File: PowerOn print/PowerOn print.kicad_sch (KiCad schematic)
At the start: 10 parts, among them P1 USB_C_Plug_USB2.0, P2 USB_C_Plug_USB2.0, Q1 FQP27P06, Q2 2N3904, SW1 SW_DIP_x01

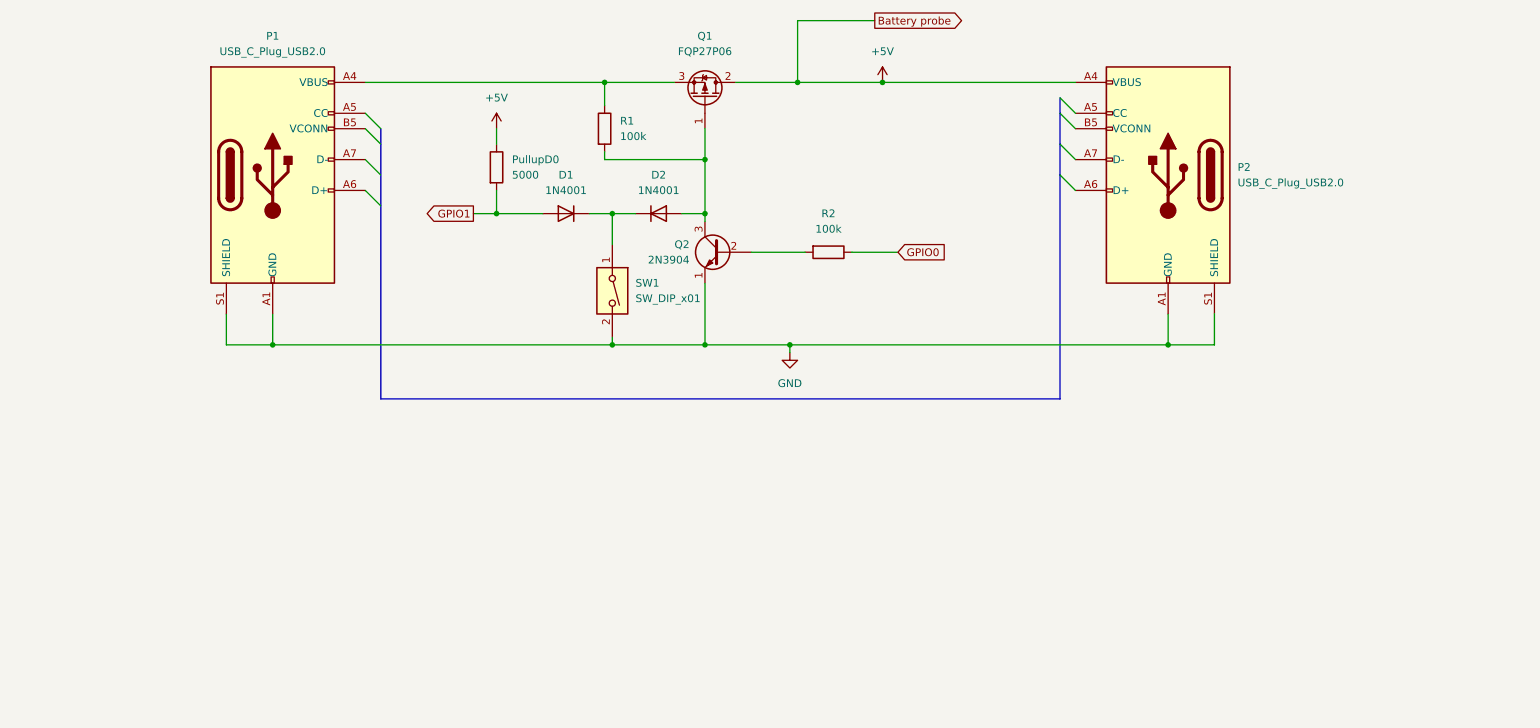
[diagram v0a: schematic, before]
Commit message: Redesign Poweron system
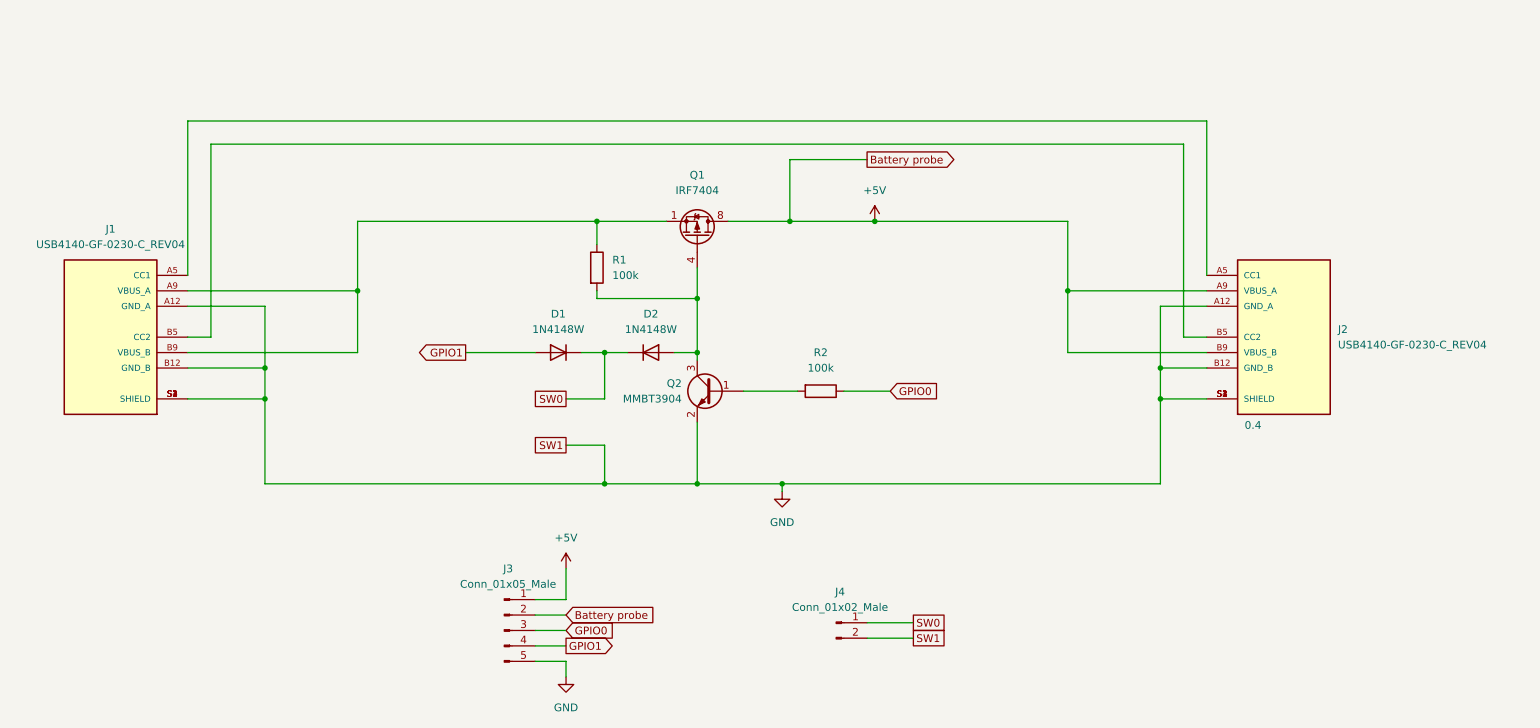
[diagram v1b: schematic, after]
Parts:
- removed D1, D2: 1N4001, Diode_THT:D_DO-41_SOD81_P10.16mm_Horizontal, symbol Diode:1N4001
- removed P1, P2: USB_C_Plug_USB2.0, symbol Connector:USB_C_Plug_USB2.0
- removed PullupD0: 5000, symbol Device:R
- removed Q1: FQP27P06, Package_TO_SOT_THT:TO-220-3_Vertical, symbol Transistor_FET:FQP27P06
- removed Q2: 2N3904, Package_TO_SOT_THT:TO-92_Inline, symbol Transistor_BJT:2N3904
- removed SW1: SW_DIP_x01, symbol Switch:SW_DIP_x01
- added D1, D2: 1N4148W, Diode_SMD:D_SOD-123, symbol Diode:1N4148W
- added J1, J2: USB4140-GF-0230-C_REV04, GCT_USB4140-GF-0230-C_REV0.4, symbol USB4140-GF-0230-C_REV0.4:USB4140-GF-0230-C_REV0.4
- added J3: Conn_01x05_Male, Connector_PinHeader_1.00mm:PinHeader_1x05_P1.00mm_Vertical, symbol Connector:Conn_01x05_Male
- added J4: Conn_01x02_Male, Connector_PinHeader_1.00mm:PinHeader_1x02_P1.00mm_Vertical, symbol Connector:Conn_01x02_Male
- added Q1: IRF7404, Package_SO:SOIC-8_3.9x4.9mm_P1.27mm, symbol Transistor_FET:IRF7404
- added Q2: MMBT3904, Package_TO_SOT_SMD:SOT-23, symbol Transistor_BJT:MMBT3904
- R1, R2: footprint (none) -> Resistor_SMD:R_0805_2012Metric
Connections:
- net +5V: now also J2.A9 (VBUS_A), J2.B9 (VBUS_B), J3.1 (Pin_1), J3.2 (Pin_2), Q1.5 (D), Q1.6 (D), Q1.7 (D), Q1.8 (D)
- net GND: now also J1.A12 (GND_A), J1.B12 (GND_B), J1.S1 (SHIELD), J1.S2 (SHIELD), J1.S3 (SHIELD), J1.S4 (SHIELD), J2.A12 (GND_A), J2.B12 (GND_B), J2.S1 (SHIELD), J2.S2 (SHIELD), J2.S3 (SHIELD), J2.S4 (SHIELD), J3.5 (Pin_5), J4.2 (Pin_2), Q2.2 (E)
- net GPIO0: now also J3.3 (Pin_3)
- net GPIO1: now also D1.2 (A), J3.4 (Pin_4)
- net at R1.2: now also D2.2 (A), Q1.4 (G), Q2.3 (C)
- net at R1.1: now also J1.A9 (VBUS_A), J1.B9 (VBUS_B), Q1.1 (S), Q1.2 (S), Q1.3 (S)
- net at R2.2: now also Q2.1 (B)
- new net: J1.A5 (CC1), J2.A5 (CC1)
- new net: J1.B5 (CC2), J2.B5 (CC2)
- new net SW0: D1.1 (K), D2.1 (K), J4.1 (Pin_1)
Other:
- moved on the sheet: R1, R2

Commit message: PCB-Poweron-print-only
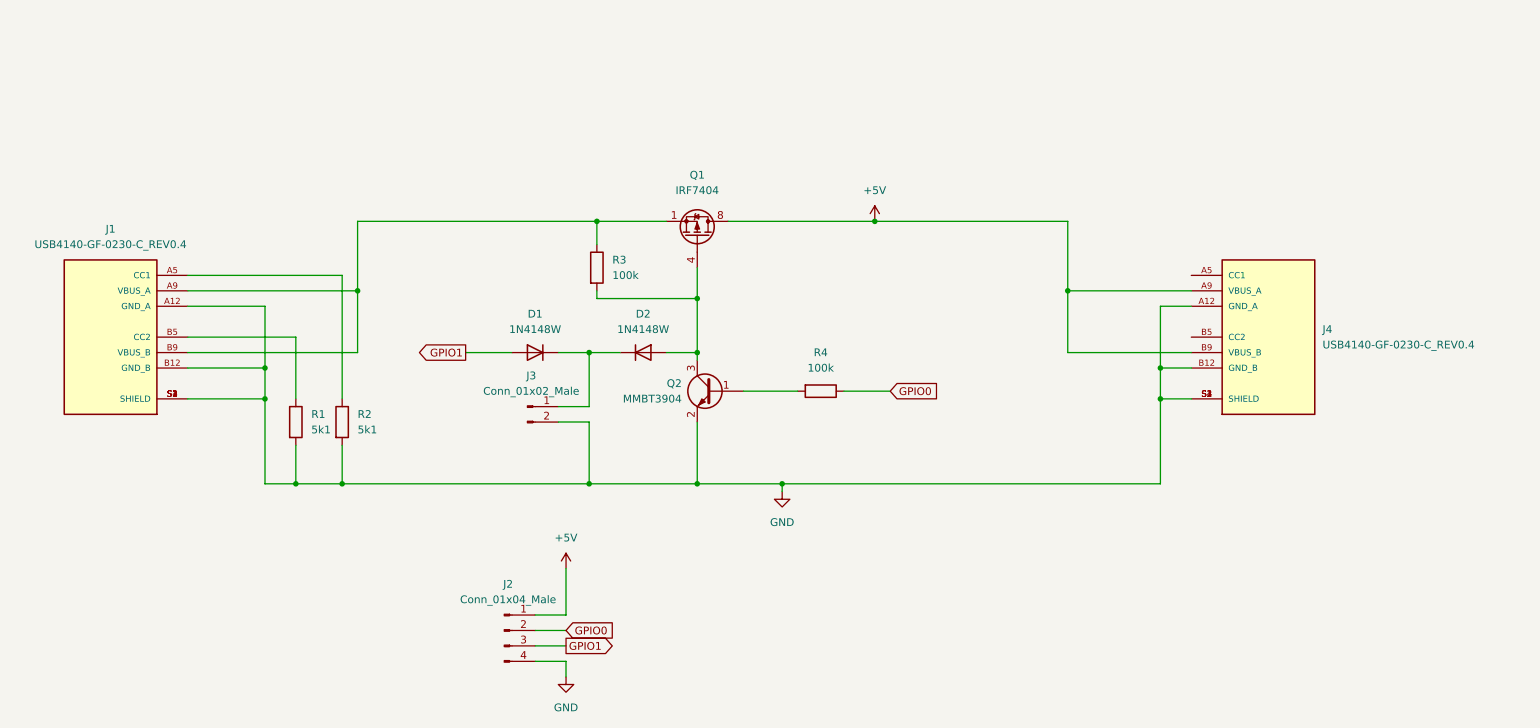
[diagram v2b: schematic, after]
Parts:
- removed J2: USB4140-GF-0230-C_REV04, GCT_USB4140-GF-0230-C_REV0.4, symbol USB4140-GF-0230-C_REV0.4:USB4140-GF-0230-C_REV0.4
- removed J3: Conn_01x05_Male, Connector_PinHeader_1.00mm:PinHeader_1x05_P1.00mm_Vertical, symbol Connector:Conn_01x05_Male
- added J2: Conn_01x04_Male, Connector_PinHeader_2.54mm:PinHeader_1x04_P2.54mm_Vertical, symbol Connector:Conn_01x04_Male
- added J4: USB4140-GF-0230-C_REV0.4, GCT_USB4140-GF-0230-C_REV0.4, symbol USB4140-GF-0230-C_REV0.4:USB4140-GF-0230-C_REV0.4
- added R1, R2: 5k1, Resistor_SMD:R_0805_2012Metric, symbol Device:R
- J1: value USB4140-GF-0230-C_REV04 -> USB4140-GF-0230-C_REV0.4
- J3: renamed from J4; footprint Connector_PinHeader_1.00mm:PinHeader_1x02_P1.00mm_Vertical -> Connector_PinHeader_2.54mm:PinHeader_1x02_P2.54mm_Vertical
- renumbered R1 to R3, R2 to R4
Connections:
- net +5V: now also J2.1 (Pin_1), J4.A9 (VBUS_A), J4.B9 (VBUS_B)
- net GND: now also J2.4 (Pin_4), J4.A12 (GND_A), J4.B12 (GND_B), J4.S1 (SHIELD), J4.S2 (SHIELD), J4.S3 (SHIELD), J4.S4 (SHIELD), R1.2, R2.2
- net GPIO0: now also J2.2 (Pin_2)
- net GPIO1: now also J2.3 (Pin_3)
- net at J1.A5 (CC1): now also R2.1
- net at J1.B5 (CC2): now also R1.1
- net SW0: no longer names the net of D1.1 (K), D2.1 (K), J3.1 (Pin_1)
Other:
- moved on the sheet: D1, D2, J3

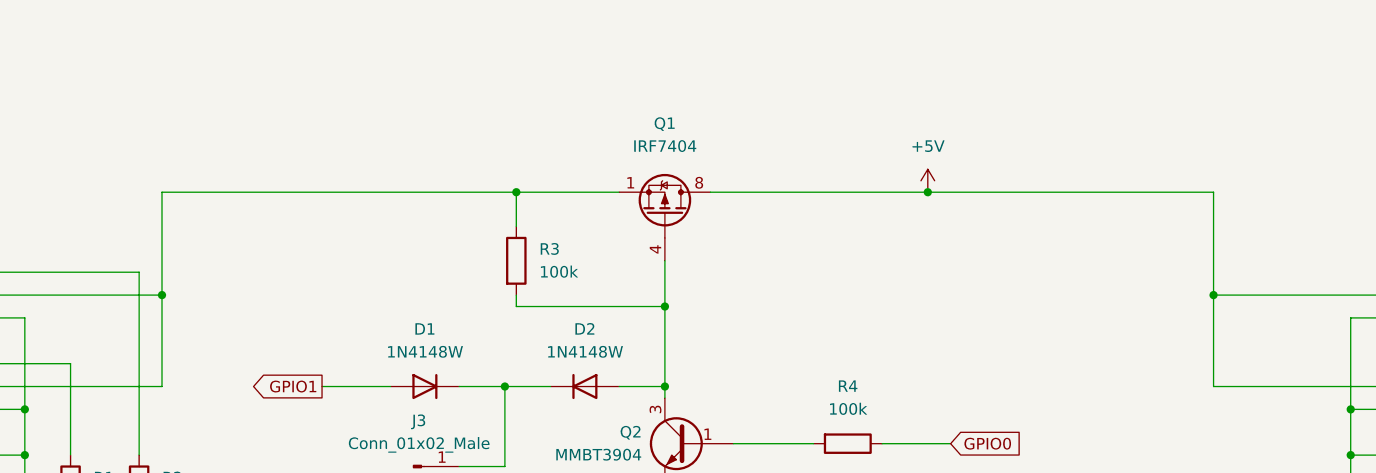
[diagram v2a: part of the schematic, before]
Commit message: Poweron print adapted
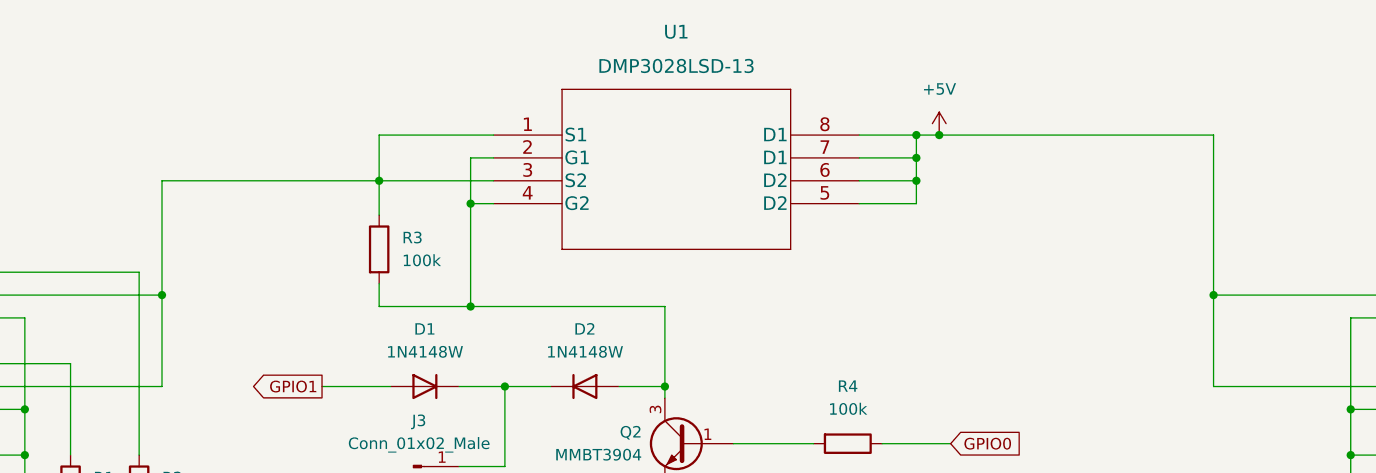
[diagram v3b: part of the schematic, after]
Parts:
- removed Q1: IRF7404, Package_SO:SOIC-8_3.9x4.9mm_P1.27mm, symbol Transistor_FET:IRF7404
- added U1: DMP3028LSD-13, footprints:DMP3028LSD-13, symbol 2023-01-28_23-14-05:DMP3028LSD-13
- J1, J4: footprint GCT_USB4140-GF-0230-C_REV0.4 -> USB4140-GF-0230-C_REV0:GCT_USB4140-GF-0230-C_REV0.4
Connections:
- net +5V: now also U1.5 (D2), U1.6 (D2), U1.7 (D1), U1.8 (D1)
- net at J1.A9 (VBUS_A), J1.B9 (VBUS_B), R3.1: now also U1.1 (S1), U1.3 (S2)
- net at D2.2 (A), Q2.3 (C), R3.2: now also U1.2 (G1), U1.4 (G2)
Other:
- moved on the sheet: R3
